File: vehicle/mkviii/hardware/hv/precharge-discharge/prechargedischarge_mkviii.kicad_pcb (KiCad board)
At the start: 2 copper layers, 158.4 x 109.4 mm, 103 parts, among them J2 Conn_01x03_Pin, J3 CONN_pcie_x1, J4 Conn_01x03_Pin, K1 G2RG-2A-X_DC12, K2 3350-4275-126, K3 G2RG-2A-X_DC12, Q1 SSM3K333R, Q2 SSM3K333R, U1 U_GATE_SN74LVC1G02DBVR, U10 SN74LVC1G08DBVR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

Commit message: Added Production Files; corrected various things in silkscreen and schematics
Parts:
- removed the G*** at (88.6, 89.6)
- added G***: LOGO, LOGO, F.Cu at (179.4, 94.3)
- moved kibuzzard-6784D6E2 27.6 mm to (186.0, 88.6)
- moved G*** 12.1 mm to (198.6, 94.2)
- moved C8 0.80 mm to (195.6, 63.5)
- moved R23 0.80 mm to (193.7, 63.5)
- moved C7 0.20 mm to (202.0, 65.1)
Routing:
- net Net-(K3-COM_(+)): track 43.0 -> 46.2 mm
- net Net-(D9-A): track 11.8 -> 10.5 mm
- net /HV_TS-: track 9.70 -> 8.81 mm

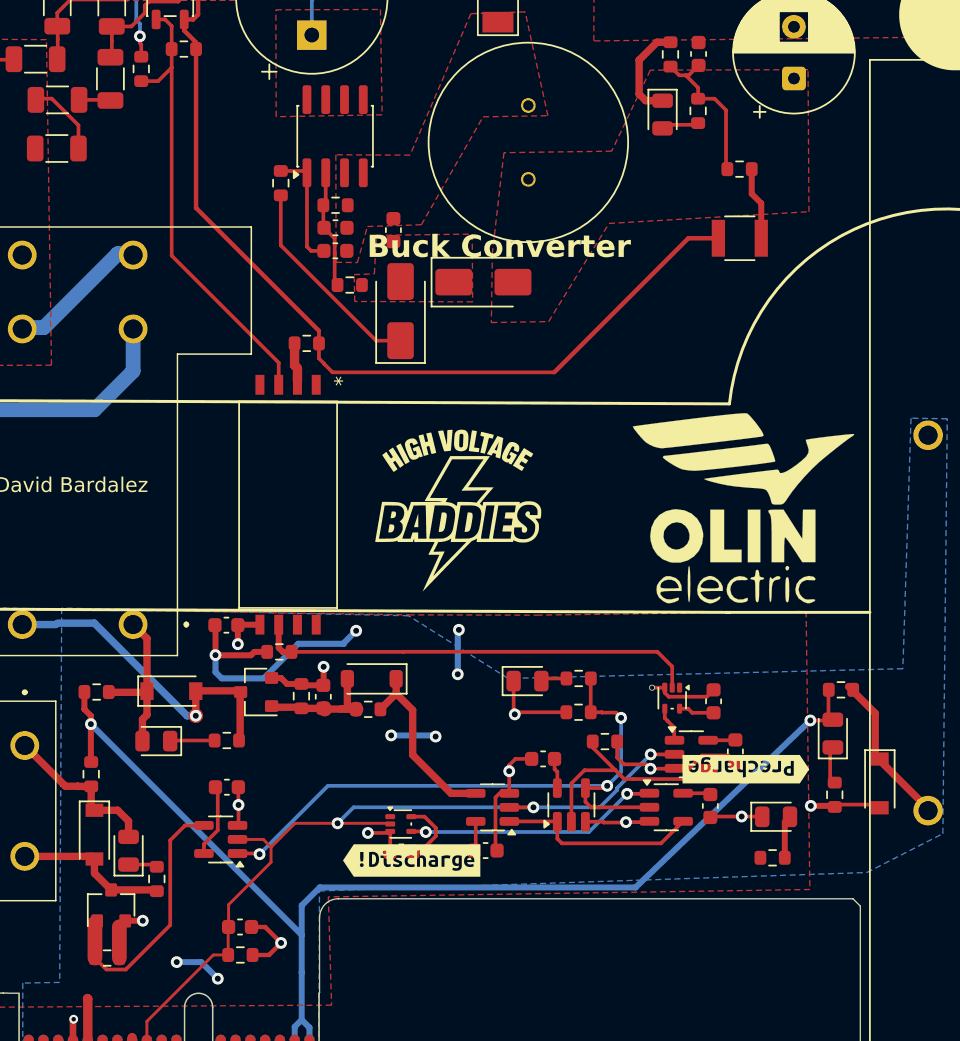
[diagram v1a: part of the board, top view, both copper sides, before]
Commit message: Precharge-discharge Renaming for BOM
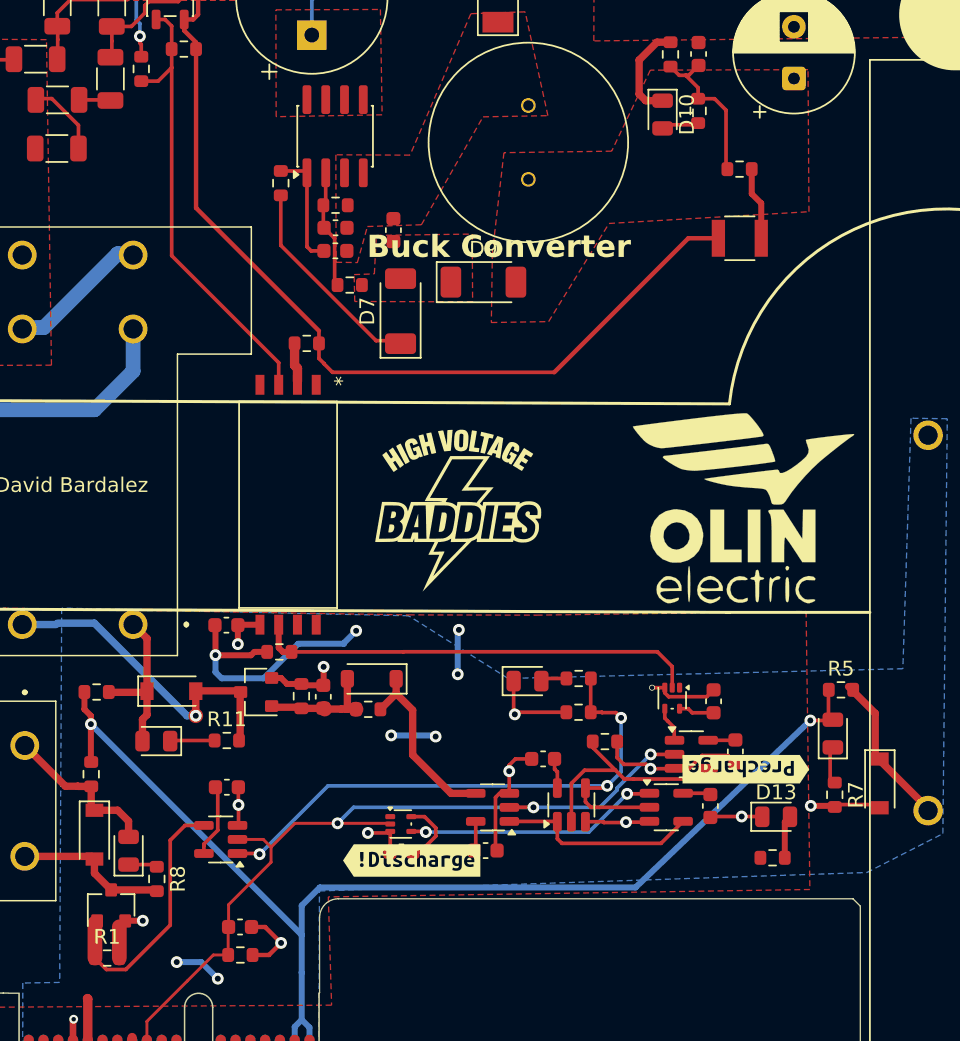
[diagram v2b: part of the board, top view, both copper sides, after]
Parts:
- C11: value C_2.2uF_25V -> C_2.2uF
- C12, C13: value C_0.1uF -> 0.1 µF
- C17: value C_10nF -> C_1uF
- D10, D13: footprint LED_SMD:LED_0805_2012Metric -> OEM:D_0805_2012Metric
- D12: value BSPD_TRIP_LED -> LED_WHITE
- D7, D9: footprint Diode_SMD:D_SMA -> OEM:D_SOD-128
- R1: value 10KR -> R_10K; footprint OEM:R_0603 -> OEM:R_0603_1608Metric
- R11, R5, R7, R8: footprint OEM:R_0603 -> OEM:R_0603_1608Metric
- R24, R27, R30: value R_1K -> 1KR
